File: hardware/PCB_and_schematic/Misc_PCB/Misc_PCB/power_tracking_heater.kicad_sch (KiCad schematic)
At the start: 9 parts, among them J6 PROG_INTERFACE, Q13 BC817, Q14 BC817, U9 ESP-07

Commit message: progress with esp power pcb
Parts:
- added C17: 22n/250V AC, symbol Device:C
- added D14, D15, D16, D17: 3V3, symbol Device:D_Zener
- added D18, D19: LED, LED_SMD:LED_PLCC-2_3.4x3.0mm_KA, symbol Device:LED
- added J13: 230V AC, symbol Connector:Screw_Terminal_01x04
- added J15: DS18B20, symbol Connector_Generic:Conn_01x03
- added J16: DISPLAY, symbol Connector_Generic:Conn_01x05
- added J17: PUSH_BUTTON, symbol Connector_Generic:Conn_01x03
- added Q15: BC817, TO_SOT_Packages_SMD:SOT-23_Handsoldering, symbol Transistor_BJT:BC817
- added Q16: BT139-600, Package_TO_SOT_THT:TO-220-3_Vertical, symbol Triac_Thyristor:BT139-600
- added Q17, Q18: BC807, Package_TO_SOT_SMD:SOT-23, symbol Transistor_BJT:BC807
- added R47, R61, R62: 10k, Resistors_SMD:R_0805_HandSoldering, symbol Device:R
- added R48: 47k, Resistors_SMD:R_0805_HandSoldering, symbol Device:R
- added R49: 47R, Resistors_SMD:R_0805_HandSoldering, symbol Device:R
- added R52, R55, R56, R57: 200R, Resistor_THT:R_Axial_DIN0204_L3.6mm_D1.6mm_P7.62mm_Horizontal, symbol Device:R
- added R53, R54: 560R, Resistors_SMD:R_0805_HandSoldering, symbol Device:R
- added R58: 390R, Resistor_THT:R_Axial_DIN0204_L3.6mm_D1.6mm_P7.62mm_Horizontal, symbol Device:R
- added R59, R60: 1k, Resistors_SMD:R_0805_HandSoldering, symbol Device:R
- added R63, R65: 10K, Resistor_SMD:R_0805_2012Metric_Pad1.20x1.40mm_HandSolder, symbol Device:R
- added R64, R66: 220R, Resistor_SMD:R_0805_2012Metric_Pad1.20x1.40mm_HandSolder, symbol Device:R
- added U12: MOC3033M, symbol Relay_SolidState:MOC3033M
- R44: value R -> 10k
- renumbered J6 to J14, R48 to R45, R47 to R46, R45 to R50, R46 to R51, U9 to U11
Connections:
- net +3V3: now also J15.3 (Pin_3), J16.5 (Pin_5), Q17.2 (E), Q18.2 (E), R61.1, R62.2, U12.1
- net DTR: now also R53.2; no longer Q14.2 (E), R50.2
- net GND: now also D14.2 (A), D15.2 (A), D16.2 (A), D17.2 (A), J15.1 (Pin_1), J16.4 (Pin_4), J17.1 (Pin_1), Q15.2 (E), R48.1, R64.1, R66.1
- net RTS: now also R54.2; no longer Q13.2 (E), R51.2
- net RXD: now also D17.1 (K), R60.1, R65.2; no longer J14.2 (Pin_2)
- net TXD: now also D16.1 (K), R59.1, R63.2; no longer J14.1 (Pin_1)
- net PUSH_BUTTON_1: now reaches U11.11 (GPIO2)
- net PUSH_BUTTON_1: now also J17.3 (Pin_3), R62.1
- net AC_POWER_DRIVE: now reaches U11.13 (GPIO4)
- net AC_POWER_DRIVE: now also R47.1
- net DS18B20: now reaches U11.14 (GPIO5)
- net DS18B20: now also J15.2 (Pin_2), R61.2
- net PUSH_BUTTON_2: now reaches U11.2 (ADC)
- net PUSH_BUTTON_2: now also J17.2 (Pin_2)
- net CS: now reaches U11.4 (GPIO16)
- net CS: now also J16.1 (Pin_1)
- net CLK: now reaches U11.5 (GPIO14)
- net CLK: now also J16.2 (Pin_2)
- net MISO: now reaches U11.6 (GPIO12)
- net MOSI: now reaches U11.7 (GPIO13)
- net MOSI: now also J16.3 (Pin_3)
- new net: Q16.3 (G), R58.1, U12.4
- new net: C17.2, J13.3 (Pin_3), J13.4 (Pin_4), Q16.1 (A1), R58.2
- new net: Q17.1 (B), R63.1
- new net: C17.1, R55.1, R56.2
- new net: R52.1, R55.2
- new net: D14.1 (K), Q14.2 (E), R50.2, R53.1
- new net: R49.1, U12.2
- new net: R52.2, U12.6
- new net: Q18.1 (B), R65.1
- new net: D19.2 (A), Q18.3 (C)
- new net: J13.1 (Pin_1), J13.2 (Pin_2), Q16.2 (A2), R57.1
- new net: D18.2 (A), Q17.3 (C)
- new net: D15.1 (K), Q13.2 (E), R51.2, R54.1
- new net: D19.1 (K), R66.2
- new net: Q15.1 (B), R47.2, R48.2
- new net: Q15.3 (C), R49.2
- new net: J14.1 (Pin_1), R59.2
- new net: J14.2 (Pin_2), R60.2
- new net: D18.1 (K), R64.2
- new net: R56.1, R57.2
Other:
- note added: "AC POWER REGUATION"
- note added: "STATUS DIODES"
- moved on the sheet: J14, Q13, Q14, R44, R45, R46, R50, R51, U11

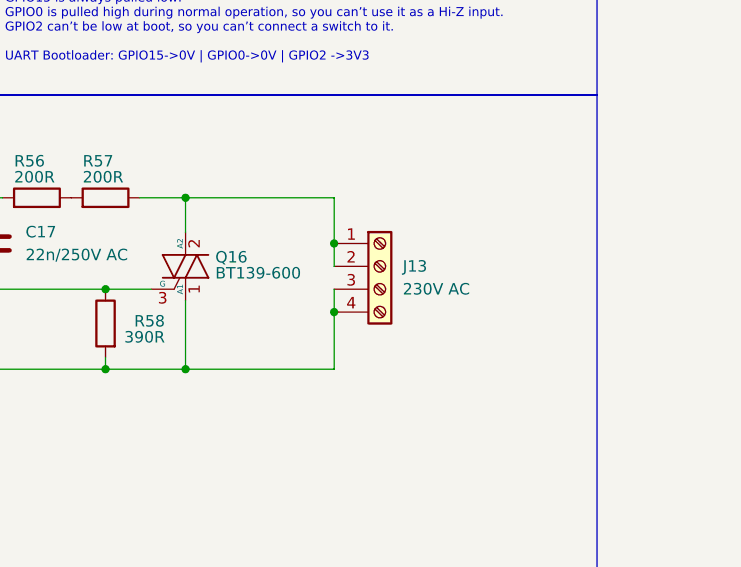
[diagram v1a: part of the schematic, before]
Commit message: add footprint association
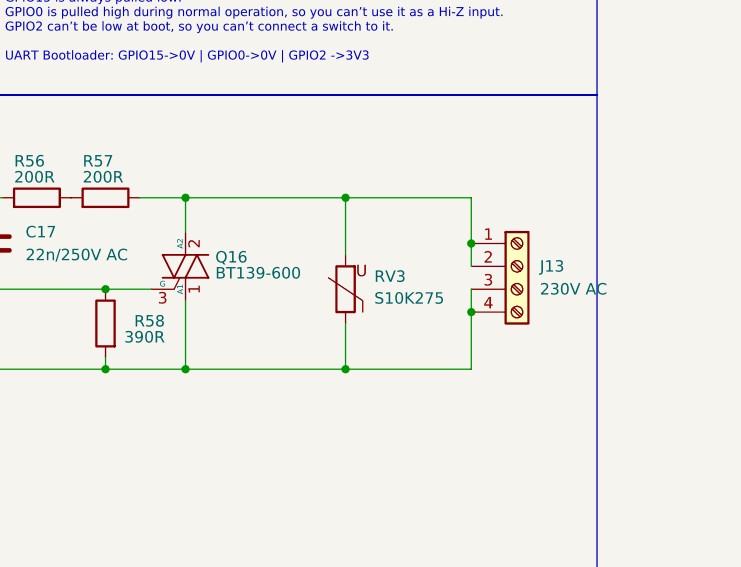
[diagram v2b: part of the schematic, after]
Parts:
- added RV3: S10K275, Varistor:RV_Disc_D7mm_W3.5mm_P5mm, symbol Device:Varistor
- C17: footprint (none) -> Capacitor_THT:C_Rect_L16.5mm_W6.0mm_P15.00mm_MKT
- D14, D15, D16, D17: footprint (none) -> Diode_SMD:D_MiniMELF
- J14: footprint (none) -> My-Footprints-connectors:Conn-01x06
- J15: footprint (none) -> Connector_JST:JST_XA_B03B-XASK-1_1x03_P2.50mm_Vertical
- J16: footprint (none) -> Connector_JST:JST_XA_B05B-XASK-1_1x05_P2.50mm_Vertical
- Q13, Q14, Q15: footprint TO_SOT_Packages_SMD:SOT-23_Handsoldering -> Package_TO_SOT_SMD:SOT-23_Handsoldering
- Q16: footprint Package_TO_SOT_THT:TO-220-3_Vertical -> My-Footprints:TO-220-3_V_Wide_Legs
- R44: footprint (none) -> Capacitor_SMD:C_0805_2012Metric
- R45, R46, R47, R48, R49, R50, R51, R53, R54, R59, R60, R61, R62: footprint Resistors_SMD:R_0805_HandSoldering -> Resistor_SMD:R_0805_2012Metric_Pad1.20x1.40mm_HandSolder
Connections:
- net at C17.2, J13.3 (Pin_3), J13.4 (Pin_4)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: now also RV3.1
- net at J13.1 (Pin_1), J13.2 (Pin_2), Q16.2 (A2)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: now also RV3.2
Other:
- moved on the sheet: J13
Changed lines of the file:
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@@
 	)
 	(junction
-		(at 254 96.52)
+		(at 269.24 104.14)
 		(diameter 0)
 		(color 0 0 0 0)
@@
 	)
 	(junction
+		(at 255.27 110.49)
+		(diameter 0)
+		(color 0 0 0 0)
+	)
+	(junction
 		(at 78.74 24.13)
 		(diameter 0)
@@
 	)
 	(junction
-		(at 189.23 57.15)
+		(at 255.27 91.44)
 		(diameter 0)
 		(color 0 0 0 0)
 	)
 	(junction
-		(at 254 104.14)
+		(at 189.23 57.15)
 		(diameter 0)
 		(color 0 0 0 0)
@@
 	)
 	(junction
+		(at 269.24 96.52)
+		(diameter 0)
+		(color 0 0 0 0)
+	)
+	(junction
 		(at 237.49 110.49)
 		(diameter 0)
@@
 	(wire
 		(pts
+			(xy 255.27 91.44) (xy 269.24 91.44)
+		)
+		(stroke
+			(width 0)
+			(type default)
+		)
+	)
+	(wire
+		(pts
 			(xy 168.91 39.37) (xy 168.91 44.45)
 		)
@@
 	(wire
 		(pts
+			(xy 255.27 91.44) (xy 255.27 97.79)
+		)
+		(stroke
+			(width 0)
+			(type default)
+		)
+	)
+	(wire
+		(pts
 			(xy 97.79 64.77) (xy 97.79 59.69)
 		)
@@
 	(wire
 		(pts
-			(xy 237.49 91.44) (xy 254 91.44)
+			(xy 237.49 91.44) (xy 255.27 91.44)
 		)
 		(stroke
@@
 	(wire
 		(pts
-			(xy 254 104.14) (xy 254 110.49)
+			(xy 269.24 104.14) (xy 269.24 110.49)
 		)
 		(stroke
@@
 	(wire
 		(pts
+			(xy 255.27 110.49) (xy 237.49 110.49)
+		)
+		(stroke
+			(width 0)
+			(type default)
+		)
+	)
+	(wire
+		(pts
 			(xy 97.79 59.69) (xy 93.98 59.69)
 		)
@@
 	(wire
 		(pts
-			(xy 254 110.49) (xy 237.49 110.49)
+			(xy 269.24 110.49) (xy 255.27 110.49)
 		)
 		(stroke
@@
 	(wire
 		(pts
-			(xy 254 91.44) (xy 254 96.52)
+			(xy 269.24 91.44) (xy 269.24 96.52)
 		)
 		(stroke
@@
 	(wire
 		(pts
+			(xy 255.27 105.41) (xy 255.27 110.49)
+		)
+		(stroke
+			(width 0)
+			(type default)
+		)
+	)
+	(wire
+		(pts
 			(xy 182.88 101.6) (xy 180.34 101.6)
 		)
@@
 	(wire
 		(pts
-			(xy 254 101.6) (xy 254 104.14)
+			(xy 269.24 101.6) (xy 269.24 104.14)
 		)
 		(stroke
@@
 	(wire
 		(pts
-			(xy 254 96.52) (xy 254 99.06)
+			(xy 269.24 96.52) (xy 269.24 99.06)
 		)
 		(stroke
@@
 			)
 		)
-		(property "Footprint" "Resistors_SMD:R_0805_HandSoldering"
+		(property "Footprint" "Resistor_SMD:R_0805_2012Metric_Pad1.20x1.40mm_HandSolder"
 			(at 99.568 68.58 90)
 			(effects
@@
 			)
 		)
-		(property "Footprint" ""
+		(property "Footprint" "Connector_JST:JST_XA_B03B-XASK-1_1x03_P2.50mm_Vertical"
 			(at 101.6 99.06 0)
 			(effects
@@
 			)
 		)
-		(property "Footprint" "Resistors_SMD:R_0805_HandSoldering"
+		(property "Footprint" "Resistor_SMD:R_0805_2012Metric_Pad1.20x1.40mm_HandSolder"
 			(at 159.258 57.15 90)
 			(effects
@@
 			)
 		)
-		(property "Footprint" ""
+		(property "Footprint" "Connector_JST:JST_XA_B05B-XASK-1_1x05_P2.50mm_Vertical"
 			(at 64.77 100.33 0)
 			(effects
@@
 			)
 		)
-		(property "Footprint" ""
+		(property "Footprint" "Diode_SMD:D_MiniMELF"
 			(at 241.3 33.02 0)
 			(effects
@@
 			)
 		)
-		(property "Footprint" "TO_SOT_Packages_SMD:SOT-23_Handsoldering"
+		(property "Footprint" "Package_TO_SOT_SMD:SOT-23_Handsoldering"
 			(at 166.37 55.245 0)
 			(effects
@@
 			)
 		)
-		(property "Footprint" ""
+		(property "Footprint" "Diode_SMD:D_MiniMELF"
 			(at 241.3 49.53 0)
 			(effects
@@
 			)
 		)
-		(property "Footprint" ""
+		(property "Footprint" "Capacitor_THT:C_Rect_L16.5mm_W6.0mm_P15.00mm_MKT"
 			(at 216.8652 100.33 0)
 			(effects
@@
 			)
 		)
-		(property "Footprint" "Resistors_SMD:R_0805_HandSoldering"
+		(property "Footprint" "Resistor_SMD:R_0805_2012Metric_Pad1.20x1.40mm_HandSolder"
 			(at 181.61 32.512 90)
 			(effects
@@
 			)
 		)
-		(property "Footprint" "Package_TO_SOT_THT:TO-220-3_Vertical"
+		(property "Footprint" "My-Footprints:TO-220-3_V_Wide_Legs"
 			(at 242.57 100.965 0)
 			(effects
@@
 			)
 		)
-		(property "Footprint" "Resistors_SMD:R_0805_HandSoldering"
+		(property "Footprint" "Resistor_SMD:R_0805_2012Metric_Pad1.20x1.40mm_HandSolder"
 			(at 204.47 55.372 90)
 			(effects
@@
 			)
 		)
-		(property "Footprint" "TO_SOT_Packages_SMD:SOT-23_Handsoldering"
+		(property "Footprint" "Package_TO_SOT_SMD:SOT-23_Handsoldering"
 			(at 182.88 118.745 0)
 			(effects
@@
 			)
 		)
-		(property "Footprint" ""
+		(property "Footprint" "My-Footprints-connectors:Conn-01x06"
 			(at 276.86 34.29 0)
 			(effects
@@
 	)
 	(symbol
+		(lib_id "Device:Varistor")
+		(at 255.27 101.6 180)
+		(unit 1)
+		(exclude_from_sim no)
+		(in_bom yes)
+		(on_board yes)
+		(dnp no)
+		(property "Reference" "RV3"
+			(at 258.4594 100.1944 0)
+			(effects
+				(font
+					(size 1.27 1.27)
+				)
+				(justify right)
+			)
+		)
+		(property "Value" "S10K275"
+			(at 258.4594 102.6187 0)
+			(effects
+				(font
+					(size 1.27 1.27)
+				)
+				(justify right)
+			)
+		)
+		(property "Footprint" "Varistor:RV_Disc_D7mm_W3.5mm_P5mm"
+			(at 257.048 101.6 90)
+			(effects
+				(font
+					(size 1.27 1.27)
+				)
+				(hide yes)
+			)
+		)
+		(property "Datasheet" "~"
+			(at 255.27 101.6 0)
+			(effects
+				(font
+					(size 1.27 1.27)
+				)
+				(hide yes)
+			)
+		)
+		(property "Description" "Voltage dependent resistor"
+			(at 255.27 101.6 0)
+			(effects
+				(font
+					(size 1.27 1.27)
+				)
+				(hide yes)
+			)
+		)
+		(property "Sim.Name" "kicad_builtin_varistor"
+			(at 255.27 101.6 0)
+			(effects
+				(font
+					(size 1.27 1.27)
+				)
+				(hide yes)
+			)
+		)
+		(property "Sim.Device" "SUBCKT"
+			(at 255.27 101.6 0)
+			(effects
+				(font
+					(size 1.27 1.27)
+				)
+				(hide yes)
+			)
+		)
+		(property "Sim.Pins" "1=A 2=B"
+			(at 255.27 101.6 0)
+			(effects
+				(font
+					(size 1.27 1.27)
+				)
+				(hide yes)
+			)
+		)
+		(property "Sim.Params" "threshold=1k"
+			(at 255.27 101.6 0)
+			(effects
+				(font
+					(size 1.27 1.27)
+				)
+				(hide yes)
+			)
+		)
+		(property "Sim.Library" "${KICAD7_SYMBOL_DIR}/Simulation_SPICE.sp"
+			(at 255.27 101.6 0)
+			(effects
+				(font
+					(size 1.27 1.27)
+				)
+				(hide yes)
+			)
+		)
+		(pin "1"
+		)
+		(pin "2"
+		)
+		(instances
+			(project "Misc_PCB"
+				(path "/7b59bc46-701c-4caa-9db8-f0eec290561d/5708feb1-aa6a-4b62-bc86-35f6572d752c"
+					(reference "RV3")
+					(unit 1)
+				)
+			)
+		)
+	)
+	(symbol
 		(lib_id "Device:R")
 		(at 114.3 95.25 0)
@@
 			)
 		)
-		(property "Footprint" "Resistors_SMD:R_0805_HandSoldering"
+		(property "Footprint" "Resistor_SMD:R_0805_2012Metric_Pad1.20x1.40mm_HandSolder"
 			(at 116.078 95.25 90)
 			(effects
@@
 			)
 		)
-		(property "Footprint" "Resistors_SMD:R_0805_HandSoldering"
+		(property "Footprint" "Resistor_SMD:R_0805_2012Metric_Pad1.20x1.40mm_HandSolder"
 			(at 181.61 55.372 90)
 			(effects
@@
 			)
 		)
-		(property "Footprint" "Resistors_SMD:R_0805_HandSoldering"
+		(property "Footprint" "Resistor_SMD:R_0805_2012Metric_Pad1.20x1.40mm_HandSolder"
 			(at 248.92 27.432 90)
 			(effects
@@
 			)
 		)
-		(property "Footprint" "Resistors_SMD:R_0805_HandSoldering"
+		(property "Footprint" "Resistor_SMD:R_0805_2012Metric_Pad1.20x1.40mm_HandSolder"
 			(at 163.83 115.062 90)
 			(effects
@@
 			)
 		)
-		(property "Footprint" ""
+		(property "Footprint" "Diode_SMD:D_MiniMELF"
 			(at 196.85 60.96 0)
 			(effects
@@
 			)
 		)
-		(property "Footprint" ""
+		(property "Footprint" "Diode_SMD:D_MiniMELF"
 			(at 196.85 38.1 0)
 			(effects
@@
 			)
 		)
-		(property "Footprint" "Resistors_SMD:R_0805_HandSoldering"
+		(property "Footprint" "Resistor_SMD:R_0805_2012Metric_Pad1.20x1.40mm_HandSolder"
 			(at 182.118 106.68 90)
 			(effects
@@
 			)
 		)
-		(property "Footprint" "Resistors_SMD:R_0805_HandSoldering"
+		(property "Footprint" "Resistor_SMD:R_0805_2012Metric_Pad1.20x1.40mm_HandSolder"
 			(at 248.92 43.942 90)
 			(effects
@@
 			)
 		)
-		(property "Footprint" "Resistors_SMD:R_0805_HandSoldering"
+		(property "Footprint" "Resistor_SMD:R_0805_2012Metric_Pad1.20x1.40mm_HandSolder"
 			(at 112.522 35.56 90)
 			(effects
@@
 	(symbol
 		(lib_id "Connector:Screw_Terminal_01x04")
-		(at 259.08 99.06 0)
+		(at 274.32 99.06 0)
 		(unit 1)
 		(exclude_from_sim no)
@@
 		(fields_autoplaced yes)
 		(property "Reference" "J13"
-			(at 261.62 99.0599 0)
+			(at 276.86 99.0599 0)
 			(effects
 				(font
@@
 		)
 		(property "Value" "230V AC"
-			(at 261.62 101.5999 0)
+			(at 276.86 101.5999 0)
 			(effects
 				(font
@@
 		)
 		(property "Footprint" ""
-			(at 259.08 99.06 0)
+			(at 274.32 99.06 0)
 			(effects
 				(font
@@
 		)
 		(property "Datasheet" "~"
-			(at 259.08 99.06 0)
+			(at 274.32 99.06 0)
 			(effects
 				(font
@@
 		)
 		(property "Description" "Generic screw terminal, single row, 01x04, script generated (kicad-library-utils/schlib/autogen/connector/)"
-			(at 259.08 99.06 0)
+			(at 274.32 99.06 0)
 			(effects
 				(font
@@
 			)
 		)
-		(property "Footprint" "Resistors_SMD:R_0805_HandSoldering"
+		(property "Footprint" "Resistor_SMD:R_0805_2012Metric_Pad1.20x1.40mm_HandSolder"
 			(at 168.402 123.19 90)
 			(effects
@@
 			)
 		)
-		(property "Footprint" "TO_SOT_Packages_SMD:SOT-23_Handsoldering"
+		(property "Footprint" "Package_TO_SOT_SMD:SOT-23_Handsoldering"
 			(at 166.37 36.195 0)
 			(effects
@@
 			)
 		)
-		(property "Footprint" ""
+		(property "Footprint" "Capacitor_SMD:C_0805_2012Metric"
 			(at 59.182 30.48 90)
 			(effects
@@
 			)
 		)
-		(property "Footprint" "Resistors_SMD:R_0805_HandSoldering"
+		(property "Footprint" "Resistor_SMD:R_0805_2012Metric_Pad1.20x1.40mm_HandSolder"
 			(at 204.47 32.512 90)
 			(effects

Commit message: update power tracking heater
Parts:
- added C23: 470u/6,3V, Capacitor_SMD:CP_Elec_5x5.7, symbol Device:C_Polarized
- added C24: 100n, Capacitor_SMD:C_0805_2012Metric, symbol Device:C
- added F1: 1A, Fuse:Fuse_2010_5025Metric, symbol Device:Polyfuse
- added J15: POWER_SUPPLY, Connector_PinSocket_2.54mm:PinSocket_1x02_P2.54mm_Vertical, symbol Connector_Generic:Conn_01x02
- added R82: 10k, Resistor_SMD:R_0805_2012Metric_Pad1.20x1.40mm_HandSolder, symbol Device:R
- added U12: AMS1117-3.3, Package_TO_SOT_SMD:SOT-223-3_TabPin2, symbol Regulator_Linear:AMS1117-3.3
- J13: renamed from J17; footprint (none) -> Connector_PinSocket_2.54mm:PinSocket_1x03_P2.54mm_Vertical
- J17: renamed from J13; footprint (none) -> TerminalBlock:TerminalBlock_bornier-4_P5.08mm
- Q15: renamed from Q13; footprint Package_TO_SOT_SMD:SOT-23_Handsoldering -> Package_TO_SOT_SMD:SOT-23
- Q16: renamed from Q14; footprint Package_TO_SOT_SMD:SOT-23_Handsoldering -> Package_TO_SOT_SMD:SOT-23
- Q17: renamed from Q15; footprint Package_TO_SOT_SMD:SOT-23_Handsoldering -> Package_TO_SOT_SMD:SOT-23
- U13: renamed from U12; footprint (none) -> Package_DIP:DIP-6_W7.62mm_LongPads
- renumbered C17 to C18, D18 to D14, D19 to D15, D14 to D16, D15 to D17, D16 to D18, D17 to D19, J16 to J14, J15 to J16, J14 to J18, Q17 to Q13, Q18 to Q14, Q16 to Q18, R63 to R48, R65 to R49, R64 to R50, R66 to R51, R44 to R52, R45 to R53, R62 to R54, R61 to R55, R46 to R56, R47 to R57, R48 to R58, R49 to R59, R50 to R60, R51 to R61, R52 to R62, R53 to R63, R54 to R64, R55 to R65, R56 to R66, R57 to R67, R58 to R68, R59 to R69, R60 to R70, RV3 to RV2
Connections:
- net +3V3: now also C23.1, C24.1, R82.2, U12.2 (VO)
- net GND: now also C23.2, C24.2, J15.1 (Pin_1), U12.1 (GND)
- net PUSH_BUTTON_2: now also R82.1
- new net: F1.1, J15.2 (Pin_2)
- new net +5V: F1.2, U12.3 (VI)
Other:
- moved on the sheet: J13

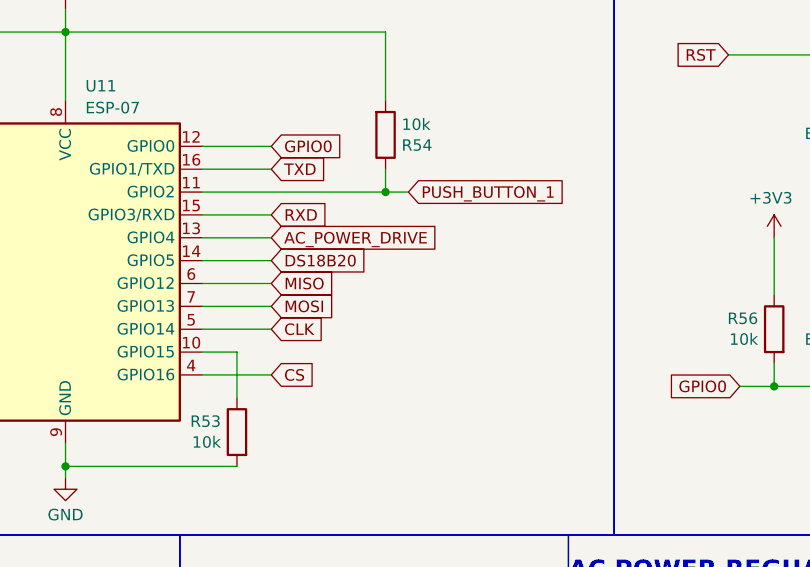
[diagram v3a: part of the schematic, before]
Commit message: Parts chage for bms
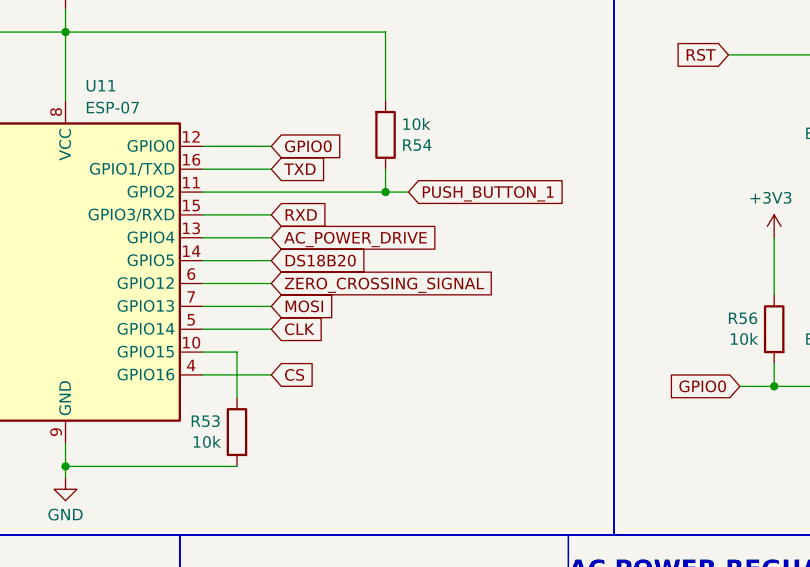
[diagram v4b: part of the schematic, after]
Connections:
- net MISO renamed ZERO_CROSSING_SIGNAL
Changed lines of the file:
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@@
 		)
 	)
-	(global_label "MISO"
+	(global_label "ZERO_CROSSING_SIGNAL"
 		(shape input)
 		(at 101.6 52.07 0)
@@
 		)
 		(property "Intersheetrefs" "${INTERSHEET_REFS}"
-			(at 109.1814 52.07 0)
+			(at 127.5057 52.07 0)
 			(effects
 				(font
